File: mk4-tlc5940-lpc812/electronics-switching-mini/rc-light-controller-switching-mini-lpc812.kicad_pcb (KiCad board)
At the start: 2 copper layers, 25 x 16 mm, 12 parts, among them J1 Conn_01x03, J2 Pinheader straight 1x06, J3 Pinheader straight 1x06, T1 PMV30UN, T2 PMV30UN, T3 PMV30UN, U1 LPC812M101JDH20, U2 MCP1703A-3302_SOT23

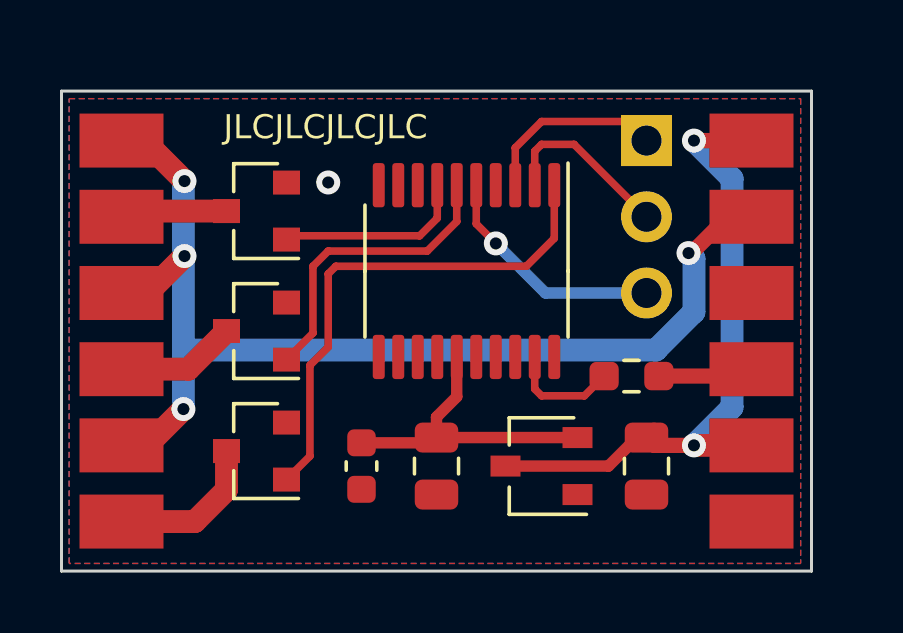
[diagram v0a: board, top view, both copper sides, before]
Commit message: Add resistor networ to protect TH-Tx/CH3/OUT-ISP
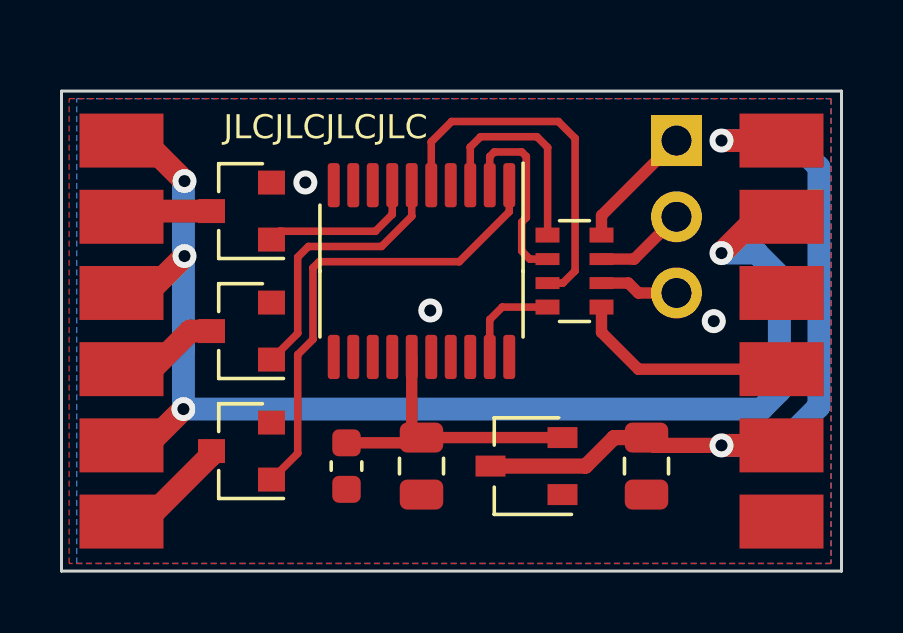
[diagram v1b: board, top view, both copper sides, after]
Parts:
- removed R1: 1k, Resistor_SMD:R_0603_1608Metric_Pad0.98x0.95mm_HandSolder
- added RN1: 1k, Resistor_SMD:R_Array_Convex_4x0603, F.Cu at (117.1, 90.0)
- moved U1 1.50 mm to (112.0, 90.0)
- moved J1 1.00 mm to (120.5, 85.7)
- moved J2 1.00 mm to (124.0, 98.3)
- moved C2 0.50 mm to (112.0, 96.5)
- moved C3 0.50 mm to (109.5, 96.5)
- moved T1 0.50 mm to (106.0, 88.0)
- moved T2 0.50 mm to (106.0, 92.0)
- moved T3 0.50 mm to (106.0, 96.0)
- moved U2 0.50 mm to (115.5, 96.5)
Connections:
- J1 pad 1: /OUT-ISP -> /OUT-ISP-in
- J1 pad 2: /CH3 -> /CH3-in
- J1 pad 3: /TH-TX -> /TH-TX-in
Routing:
- net /LED+: track 37.7 -> 44.2 mm
- net /VIN: track 22.2 -> 27.6 mm
- net /TH-TX: track 7.92 -> 12.3 mm, vias 1 -> 0
- net /OUT-ISP-in: track 0.00 -> 4.19 mm
- net /ST-Rx-in: track 3.18 -> 7.35 mm
- net /CH3-in: track 0.00 -> 3.08 mm
- net /TH-TX-in: track 0.00 -> 2.64 mm
- net /OUT0: track 17.2 -> 15.8 mm
- net Net-(J3-Pad1): track 5.23 -> 4.04 mm
- net /OUT2: track 6.42 -> 5.35 mm
- net /OUT1: track 10.1 -> 9.18 mm
- net /OUT-ISP: track 6.25 -> 7.07 mm
- net /CH3: track 5.95 -> 6.48 mm
- net Net-(J3-Pad5): track 3.58 -> 3.08 mm
- net GND: vias 1 -> 3
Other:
- board size 25 x 16 mm -> 26 x 16 mm

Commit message: Change output labels back to 0..2
16..18 may be weird as it is not in line with all the other
light controllers
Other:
- board text added: "OUT0"
- board text added: "OUT1"
- board text added: "OUT2"
- board text removed: "OUT16"
- board text removed: "OUT17"
- board text removed: "OUT18"

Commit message: Fix AUX2 and improve the layout
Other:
- board text added: "."
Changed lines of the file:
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@@
   (general
     (thickness 1.6)
-    (drawings 25)
+    (drawings 27)
     (tracks 106)
     (zones 0)
@@
     (descr "TSSOP, 20 Pin (JEDEC MO-153 Var AC https://www.jedec.org/document_search?search_api_views_fulltext=MO-153), generated with kicad-footprint-generator ipc_gullwing_generator.py")
     (tags "TSSOP SO")
+    (solder_paste_margin -0.0254)
     (attr smd)
     (fp_text reference U1 (at 0 -4.2 90) (layer F.SilkS) hide
@@
     )
   )
+  (gr_text + (at 112.0396 94.3612) (layer F.SilkS)
+    (effects (font (size 0.762 0.762) (thickness 0.1905)))
+  )
+  (gr_text . (at 114.9112 85.034) (layer F.SilkS)
+    (effects (font (size 2 2) (thickness 0.4)))
+  )
   (gr_text JLCJLCJLCJLC (at 108.8 85.2) (layer F.SilkS)

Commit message: Tweak routing and silkscreen
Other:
- board text added: "LANE Boys RC Mk4S-mini"
- board text removed: "LANE Boys RC"
- board text removed: "RC Light Controller Mk4S-mini"
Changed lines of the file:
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@@
   (general
     (thickness 1.6)
-    (drawings 27)
-    (tracks 106)
+    (drawings 26)
+    (tracks 109)
     (zones 0)
     (modules 12)
@@
     (effects (font (size 1 1) (thickness 0.2)) (justify mirror))
   )
-  (gr_text "LANE Boys RC" (at 115.4 93.5) (layer B.SilkS)
-    (effects (font (size 1 1) (thickness 0.25)) (justify mirror))
-  )
   (gr_text TH/Tx (at 119.4 90.73) (layer B.SilkS)
     (effects (font (size 1 1) (thickness 0.2)) (justify left mirror))
@@
     (effects (font (size 1 1) (thickness 0.2)) (justify left mirror))
   )
-  (gr_text "RC Light Controller\nMk4S-mini" (at 120.9 97.4) (layer B.SilkS)
-    (effects (font (size 1 1) (thickness 0.25)) (justify left mirror))
+  (gr_text "LANE Boys RC\nMk4S-mini" (at 113.4366 96.4694) (layer B.SilkS)
+    (effects (font (size 1.4 1.4) (thickness 0.3)) (justify mirror))
   )
   (gr_text OUT0 (at 100.5 98.476) (layer B.SilkS)
@@
   (segment (start 104.064 89.536) (end 104.064 92.5324) (width 0.762) (layer B.Cu) (net 7))
   (segment (start 104.064 92.5324) (end 104.064 92.634) (width 0.762) (layer B.Cu) (net 7))
-  (segment (start 123.21 88.19) (end 124 88.19) (width 0.762) (layer F.Cu) (net 7))
-  (via (at 122 89.4) (size 0.8) (drill 0.4) (layers F.Cu B.Cu) (net 7))
-  (segment (start 122 89.4) (end 123.21 88.19) (width 0.762) (layer F.Cu) (net 7))
+  (segment (start 123.367 88.19) (end 124 88.19) (width 0.762) (layer F.Cu) (net 7))
+  (via (at 122.1996 89.3574) (size 0.8) (drill 0.4) (layers F.Cu B.Cu) (net 7))
+  (segment (start 122.1996 89.3574) (end 123.367 88.19) (width 0.762) (layer F.Cu) (net 7))
+  (segment (start 123.3324 94.6) (end 104.064 94.6) (width 0.762) (layer B.Cu) (net 7))
   (segment (start 123.9268 94.0056) (end 123.3324 94.6) (width 0.762) (layer B.Cu) (net 7))
-  (segment (start 123.9268 90.1448) (end 123.9268 94.0056) (width 0.762) (layer B.Cu) (net 7))
-  (segment (start 123.3324 94.6) (end 104.064 94.6) (width 0.762) (layer B.Cu) (net 7))
-  (segment (start 122 89.4) (end 123.182 89.4) (width 0.762) (layer B.Cu) (net 7))
-  (segment (start 123.182 89.4) (end 123.9268 90.1448) (width 0.762) (layer B.Cu) (net 7))
+  (segment (start 123.9268 89.9162) (end 123.9268 94.0056) (width 0.762) (layer B.Cu) (net 7))
+  (segment (start 122.1996 89.3574) (end 123.368 89.3574) (width 0.762) (layer B.Cu) (net 7))
+  (segment (start 123.368 89.3574) (end 123.9268 89.9162) (width 0.762) (layer B.Cu) (net 7))
   (segment (start 118 91.2) (end 118 92.0412) (width 0.381) (layer F.Cu) (net 8))
   (segment (start 119.2288 93.27) (end 124 93.27) (width 0.381) (layer F.Cu) (net 8))
@@
   (segment (start 114.275 91.6178) (end 114.275 92.8625) (width 0.254) (layer F.Cu) (net 12))
   (segment (start 114.6928 91.2) (end 114.275 91.6178) (width 0.254) (layer F.Cu) (net 12))
-  (segment (start 107.874 96.076) (end 107 96.95) (width 0.254) (layer F.Cu) (net 13))
-  (segment (start 107.874 92.7864) (end 107.874 96.076) (width 0.254) (layer F.Cu) (net 13))
-  (segment (start 114.925 88.0214) (end 113.2588 89.6876) (width 0.254) (layer F.Cu) (net 13))
-  (segment (start 114.925 87.1375) (end 114.925 88.0214) (width 0.254) (layer F.Cu) (net 13))
-  (segment (start 108.382 89.8908) (end 108.382 92.2784) (width 0.254) (layer F.Cu) (net 13))
-  (segment (start 113.2588 89.6876) (end 108.5852 89.6876) (width 0.254) (layer F.Cu) (net 13))
-  (segment (start 108.5852 89.6876) (end 108.382 89.8908) (width 0.254) (layer F.Cu) (net 13))
-  (segment (start 108.382 92.2784) (end 107.874 92.7864) (width 0.254) (layer F.Cu) (net 13))
+  (segment (start 114.9352 87.1477) (end 114.925 87.1375) (width 0.254) (layer F.Cu) (net 13))
+  (segment (start 114.6304 88.4176) (end 114.9352 88.1128) (width 0.254) (layer F.Cu) (net 13))
+  (segment (start 110.922 89.6876) (end 112.192 88.4176) (width 0.254) (layer F.Cu) (net 13))
+  (segment (start 107.874 96.076) (end 107.874 92.7864) (width 0.254) (layer F.Cu) (net 13))
+  (segment (start 114.9352 88.1128) (end 114.9352 87.1477) (width 0.254) (layer F.Cu) (net 13))
+  (segment (start 112.192 88.4176) (end 114.6304 88.4176) (width 0.254) (layer F.Cu) (net 13))
+  (segment (start 107.874 92.7864) (end 108.382 92.2784) (width 0.254) (layer F.Cu) (net 13))
+  (segment (start 108.382 92.2784) (end 108.382 89.8908) (width 0.254) (layer F.Cu) (net 13))
+  (segment (start 108.382 89.8908) (end 108.5852 89.6876) (width 0.254) (layer F.Cu) (net 13))
+  (segment (start 107 96.95) (end 107.874 96.076) (width 0.254) (layer F.Cu) (net 13))
+  (segment (start 108.5852 89.6876) (end 110.922 89.6876) (width 0.254) (layer F.Cu) (net 13))
   (segment (start 107.874 89.5352) (end 107.874 92.076) (width 0.254) (layer F.Cu) (net 14))
   (segment (start 110.668 89.1796) (end 108.2296 89.1796) (width 0.254) (layer F.Cu) (net 14))

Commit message: Add PCB thickness remark
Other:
- board text added: "Thickness 0.8mm"
